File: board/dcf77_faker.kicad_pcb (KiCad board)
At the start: 4 copper layers, 69 x 32 mm, 50 parts, among them J1 Barrel_Jack, J2 DBG, J3 ANT, J4 LCD_I2C, SW1 RST, SW2 H, SW3 MIN, SW4 S, U1 NCP1117ST33T3G, U2 ATSAML21G18B-AUT, X1 32.768kHz, X2 31MHz

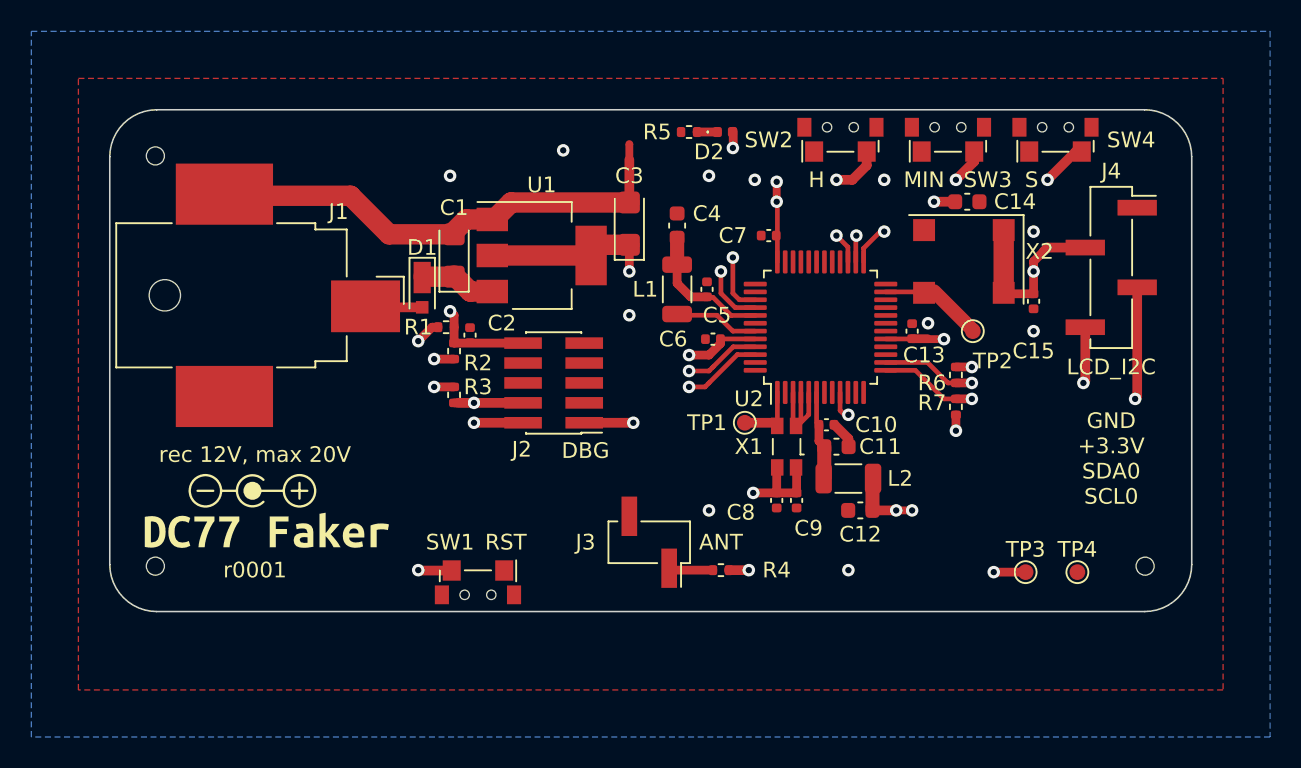
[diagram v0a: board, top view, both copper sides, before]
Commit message: hand-solder X2, fix newly-detected DRC violations
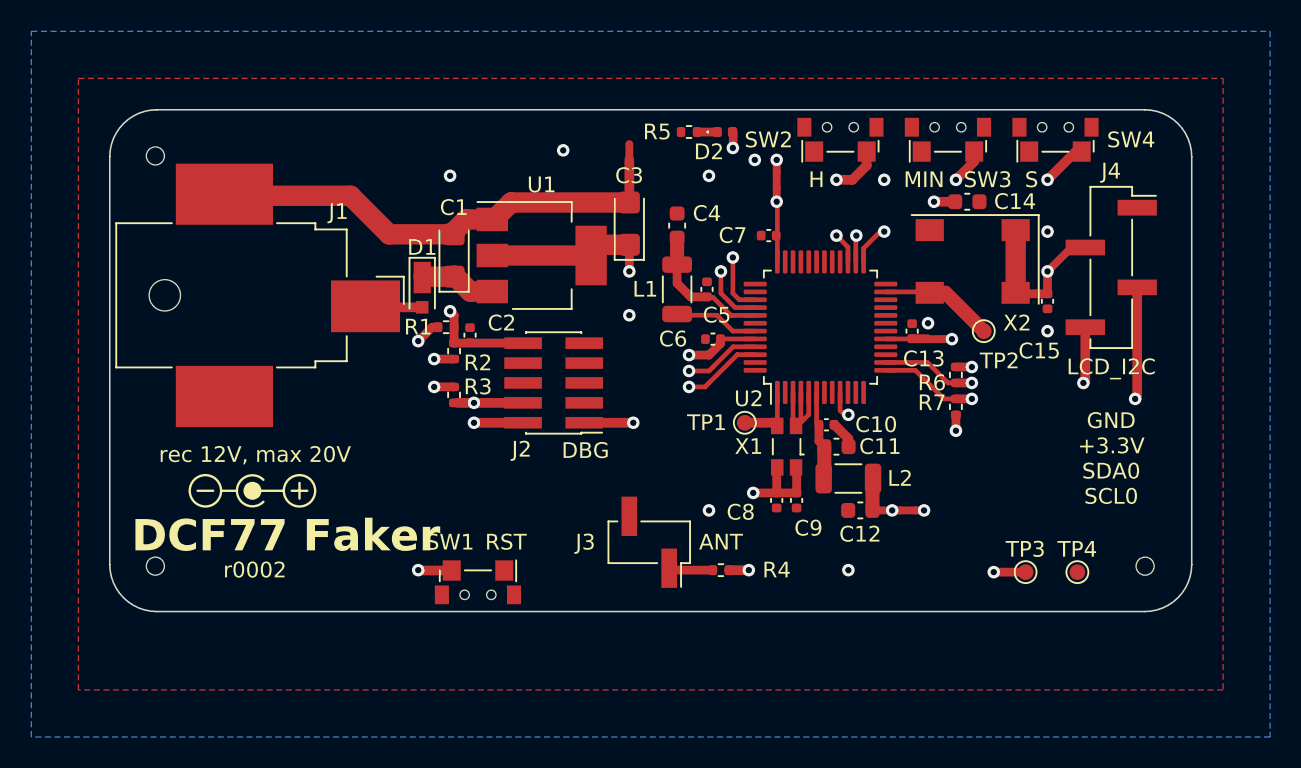
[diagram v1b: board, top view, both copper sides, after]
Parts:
- removed kibuzzard-1: G***, kibuzzard-639272B4
- X2: footprint Oscillator_Microchip:Oscillator_SMD_Microchip_DSC8001A-6Pin_7.0x5.0mm -> Oscillator_Microchip:Oscillator_SMD_Microchip_DSC8001A-6Pin_7.0x5.0mm_HandSolder
- moved C15 0.89 mm to (209.8, 69.2)
- moved NT2 0.77 mm to (192.5, 61.5)
- moved TP2 0.70 mm to (205.7, 71.1)
- moved X2 0.56 mm to (205.0, 66.7)
- moved NT3 0.24 mm to (200.9, 82.5)
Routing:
- net /VDDIO2: track 24.2 -> 25.8 mm
- net /XIN: track 5.53 -> 6.43 mm
- net +3.3V: track 37.9 -> 37.2 mm
- net /S: track 18.8 -> 19.3 mm
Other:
- board text added: "DCF77 Faker"
- board text added: "r0002"
- board text removed: "r0001"

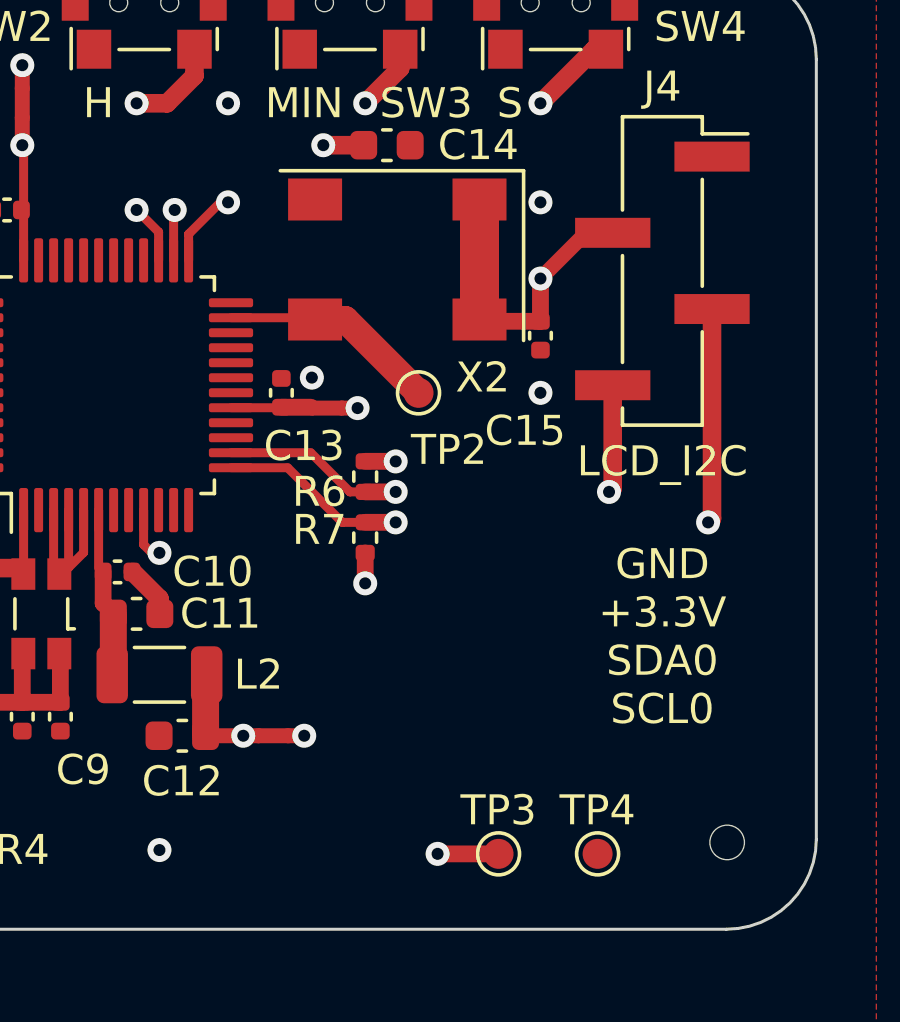
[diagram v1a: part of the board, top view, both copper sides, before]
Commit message: board: allow disabling X2
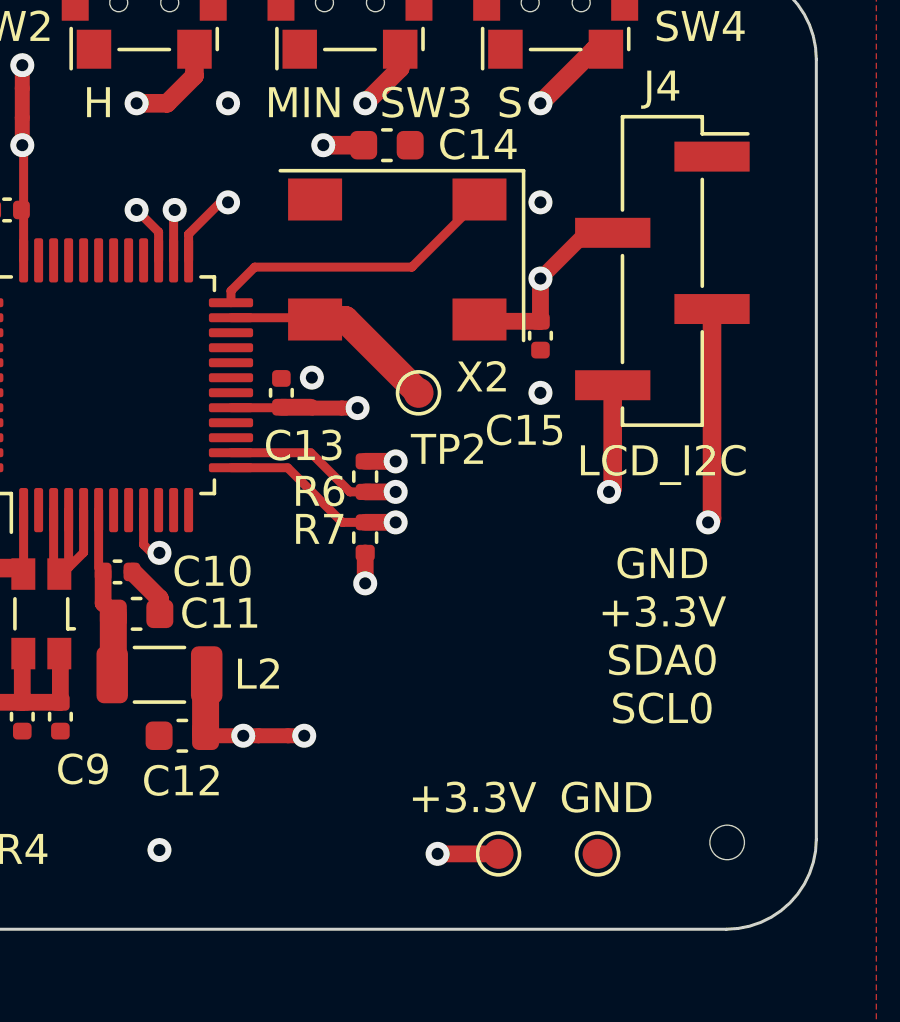
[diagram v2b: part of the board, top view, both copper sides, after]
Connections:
- U2 pad 24: unconnected-(U2-PA15-Pad24) -> /X~{ST}
- X2 pad 1: +3.3V -> /X~{ST}
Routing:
- net /X~{ST}: track 0.00 -> 9.94 mm
- net +3.3V: track 37.2 -> 33.3 mm
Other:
- board text added: "+3.3V"
- board text added: "GND"
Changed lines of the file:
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@@
   (net 3 "+3.3V")
   (net 4 "/VDDANA")
-  (net 5 "Net-(#FLG0102-pwr)")
+  (net 5 "Net-(D1-A)")
   (net 6 "Net-(D2-K)")
   (net 7 "/RAWGND")
@@
   (net 36 "unconnected-(U2-PA12-Pad21)")
   (net 37 "unconnected-(U2-PA13-Pad22)")
-  (net 38 "unconnected-(U2-PA15-Pad24)")
+  (net 38 "/X~{ST}")
   (net 39 "unconnected-(U2-PA19-Pad28)")
   (net 40 "unconnected-(U2-PA20-Pad29)")
@@
     (pad "" np_thru_hole circle (at 0 7 270) (size 2 2) (drill 2) (layers "*.Cu" "*.Mask"))
     (pad "1" smd rect (at 0.7 -5.8 270) (size 3.3 4.4) (layers "F.Cu" "F.Paste" "F.Mask")
-      (net 5 "Net-(#FLG0102-pwr)") (pintype "passive"))
+      (net 5 "Net-(D1-A)") (pintype "passive"))
     (pad "2" smd rect (at -6.45 3.2 270) (size 3.9 6.2) (layers "F.Cu" "F.Paste" "F.Mask")
       (net 7 "/RAWGND") (pintype "passive"))
@@
       (net 24 "/XIN") (pinfunction "PA14") (pintype "bidirectional"))
     (pad "24" smd roundrect (at 2.75 4.1625 90) (size 0.3 1.475) (layers "F.Cu" "F.Paste" "F.Mask") (roundrect_rratio 0.25)
-      (net 38 "unconnected-(U2-PA15-Pad24)") (pinfunction "PA15") (pintype "bidirectional+no_connect"))
+      (net 38 "/X~{ST}") (pinfunction "PA15") (pintype "bidirectional"))
     (pad "25" smd roundrect (at 4.1625 2.75 90) (size 1.475 0.3) (layers "F.Cu" "F.Paste" "F.Mask") (roundrect_rratio 0.25)
       (net 51 "/S") (pinfunction "PA16") (pintype "bidirectional"))
@@
       (net 2 "Net-(D1-K)") (pinfunction "K") (pintype "passive"))
     (pad "2" smd rect (at 1.02 0 270) (size 0.8 0.8) (layers "F.Cu" "F.Paste" "F.Mask")
-      (net 5 "Net-(#FLG0102-pwr)") (pinfunction "A") (pintype "passive"))
+      (net 5 "Net-(D1-A)") (pinfunction "A") (pintype "passive"))
     (model "${KICAD6_3DMODEL_DIR}/Diode_SMD.3dshapes/D_MicroSMP_AK.wrl"
       (offset (xyz 0 0 0))
@@
     (property "ki_keywords" "test point tp")
     (attr exclude_from_pos_files exclude_from_bom)
-    (fp_text reference "TP4" (at 0 -1.448) (layer "F.SilkS")
+    (fp_text reference "TP4" (at 0 -1.448) (layer "F.SilkS") hide
         (effects (font (size 1 1) (thickness 0.15)))
     )
@@
         (effects (font (size 1 1) (thickness 0.15)))
     )
-    (fp_text user "${REFERENCE}" (at 0 -1.45) (layer "F.Fab")
+    (fp_text user "${REFERENCE}" (at 0 1.651) (layer "F.Fab")
         (effects (font (size 1 1) (thickness 0.15)))
     )
@@
     (property "ki_keywords" "test point tp")
     (attr exclude_from_pos_files exclude_from_bom)
-    (fp_text reference "TP3" (at 0 -1.448) (layer "F.SilkS")
+    (fp_text reference "TP3" (at 0 -1.448) (layer "F.SilkS") hide
         (effects (font (size 1 1) (thickness 0.15)))
     )
@@
         (effects (font (size 1 1) (thickness 0.15)))
     )
-    (fp_text user "${REFERENCE}" (at 0 -1.45) (layer "F.Fab")
+    (fp_text user "${REFERENCE}" (at 0 1.651) (layer "F.Fab")
         (effects (font (size 1 1) (thickness 0.15)))
     )
@@
       (stroke (width 0.1) (type solid)) (layer "F.Fab"))
     (pad "1" smd rect (at -2 -2.74 270) (size 1.4 1.8) (layers "F.Cu" "F.Paste" "F.Mask")
-      (net 3 "+3.3V") (pinfunction "~{ST}") (pintype "input"))
+      (net 38 "/X~{ST}") (pinfunction "~{ST}") (pintype "input"))
     (pad "2" smd rect (at -2 2.74 270) (size 1.4 1.8) (layers "F.Cu" "F.Paste" "F.Mask")
       (net 1 "GND") (pinfunction "GND") (pintype "power_in"))
@@
     )
   )
+  (gr_text "+3.3V" (at 209.677 85.217) (layer "F.SilkS")
+    (effects (font (size 1 1) (thickness 0.15)) (justify right bottom))
+  )
   (gr_text "GND\n+3.3V\nSDA0\nSCL0" (at 213.868 79.248) (layer "F.SilkS")
     (effects (font (size 1 1) (thickness 0.15)))
@@
     (effects (font (size 1 1) (thickness 0.15)))
   )
+  (gr_text "GND" (at 210.439 85.217) (layer "F.SilkS")
+    (effects (font (size 1 1) (thickness 0.15)) (justify left bottom))
+  )
   (segment (start 193.576 75.0285) (end 193.576 76.934) (width 0.299974) (layer "F.Cu") (net 1))
   (segment (start 194.576 75.0285) (end 194.576 76.442) (width 0.299974) (layer "F.Cu") (net 1))
@@
   (segment (start 209.804 68.735) (end 207.832 68.735) (width 0.56007) (layer "F.Cu") (net 3))
   (segment (start 183.134 65.612) (end 180.768 65.612) (width 1.299972) (layer "F.Cu") (net 3))
-  (segment (start 207.772 64.675) (end 207.772 68.58) (width 1.299972) (layer "F.Cu") (net 3))
   (segment (start 193.802 81.435) (end 191.036 81.435) (width 0.56007) (layer "F.Cu") (net 3))
   (segment (start 192.532 60.96) (end 192.532 60.198) (width 0.5) (layer "F.Cu") (net 3))
@@
   (segment (start 192.576 75.0285) (end 192.576 77.045) (width 0.299974) (layer "F.Cu") (net 25))
   (segment (start 190.5 76.962) (end 192.405 76.962) (width 0.620014) (layer "F.Cu") (net 25))
+  (segment (start 199.4885 67.7195) (end 200.279 66.929) (width 0.3) (layer "F.Cu") (net 38))
+  (segment (start 205.518 66.929) (end 207.772 64.675) (width 0.3) (layer "F.Cu") (net 38))
+  (segment (start 200.279 66.929) (end 205.518 66.929) (width 0.3) (layer "F.Cu") (net 38))
+  (segment (start 199.4885 68.116) (end 199.4885 67.7195) (width 0.3) (layer "F.Cu") (net 38))
   (segment (start 191.1635 71.616) (end 188.988 71.616) (width 0.299974) (layer "F.Cu") (net 48))
   (segment (start 188.214 72.644) (end 187.198 72.644) (width 0.56007) (layer "F.Cu") (net 48))

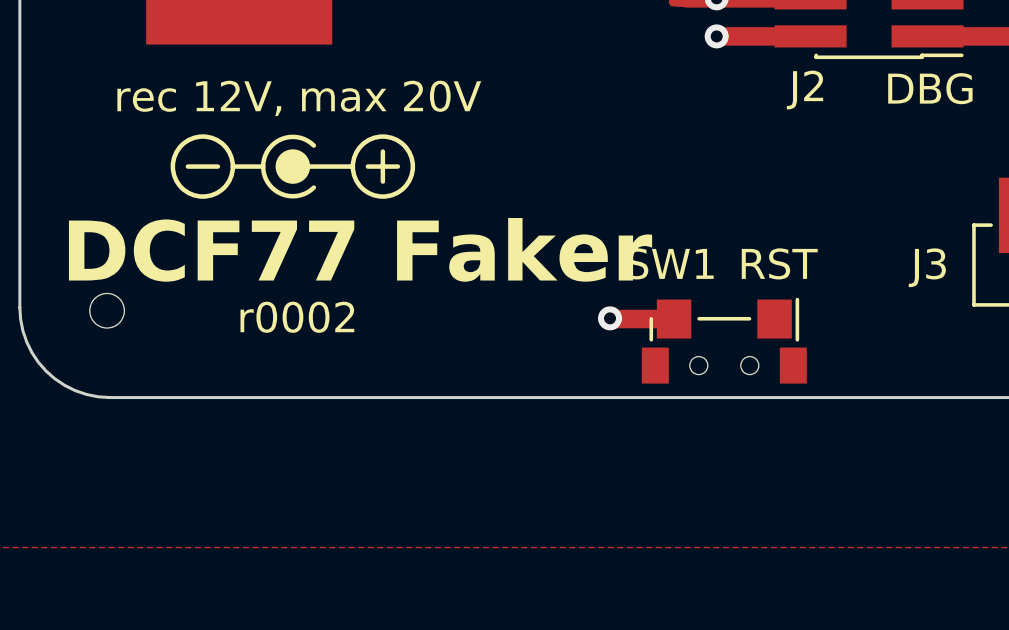
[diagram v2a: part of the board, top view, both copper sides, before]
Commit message: board: move RST to make space for battery input
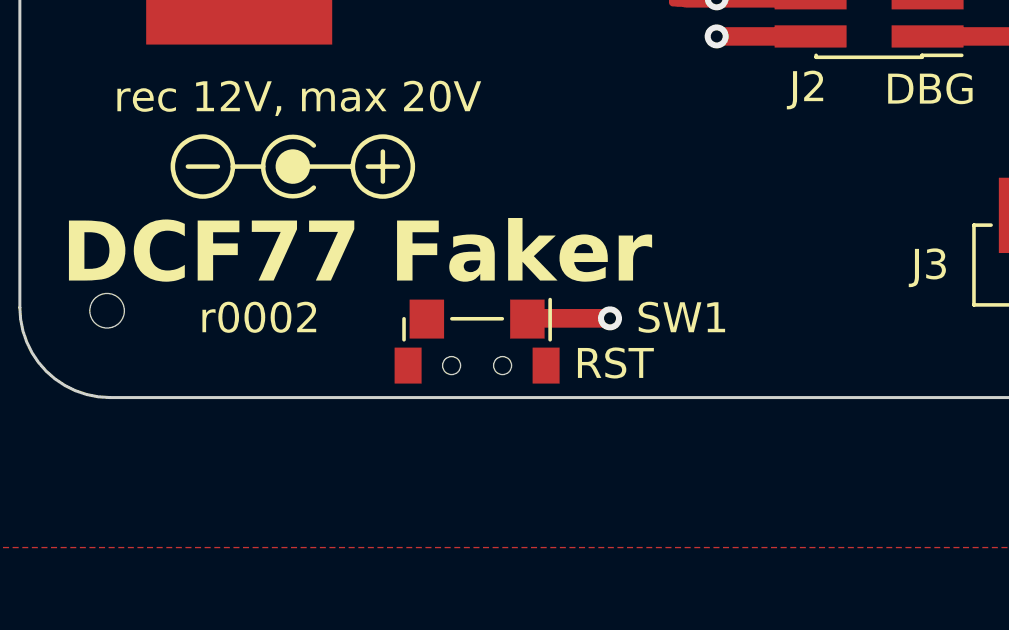
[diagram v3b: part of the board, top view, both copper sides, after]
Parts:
- moved SW1 8.24 mm to (165.2, 87.9)
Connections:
- SW1 pad 1: GND -> Net-(R2-Pad2)
- SW1 pad 2: Net-(R2-Pad2) -> GND
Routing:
- net Net-(R2-Pad2): track 17.3 -> 17.9 mm
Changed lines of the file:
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@@
   )
   (footprint "Button_Switch_SMD_Side:Shou_Han_TS24CA" (layer "F.Cu")
-    (at 173.482 87.884 180)
+    (at 165.241 87.884 180)
     (descr "Horizontal SMD button, https://datasheet.lcsc.com/lcsc/1912111437_SHOU-HAN-TS24CA_C393942.pdf")
     (property "LCSC" "C393942")
@@
     (property "ki_keywords" "switch normally-open pushbutton push-button")
     (attr smd)
-    (fp_text reference "SW1" (at 1.778 3.302 unlocked) (layer "F.SilkS")
-        (effects (font (size 1 1) (thickness 0.15)))
-    )
-    (fp_text value "RST" (at -1.778 3.302 unlocked) (layer "F.SilkS")
+    (fp_text reference "SW1" (at -6.844 1.524 unlocked) (layer "F.SilkS")
+        (effects (font (size 1 1) (thickness 0.15)))
+    )
+    (fp_text value "RST" (at -4.558 0 unlocked) (layer "F.SilkS")
         (effects (font (size 1 1) (thickness 0.15)))
     )
@@
     (pad "" np_thru_hole circle (at 0.85 -0.05 180) (size 0.6 0.6) (drill 0.6) (layers "F&B.Cu" "*.Mask"))
     (pad "1" smd rect (at -1.675 1.5 180) (size 1.15 1.3) (layers "F.Cu" "F.Paste" "F.Mask")
-      (net 1 "GND") (pinfunction "1") (pintype "passive"))
+      (net 22 "Net-(R2-Pad2)") (pinfunction "1") (pintype "passive"))
     (pad "2" smd rect (at 1.675 1.5 180) (size 1.15 1.3) (layers "F.Cu" "F.Paste" "F.Mask")
-      (net 22 "Net-(R2-Pad2)") (pinfunction "2") (pintype "passive"))
+      (net 1 "GND") (pinfunction "2") (pintype "passive"))
     (pad "3" smd rect (at -2.3 -0.05 180) (size 0.9 1.2) (layers "F.Cu" "F.Paste" "F.Mask"))
     (pad "3" smd rect (at 2.3 -0.05 180) (size 0.9 1.2) (layers "F.Cu" "F.Paste" "F.Mask"))
@@
     (effects (font (size 1 1) (thickness 0.15)))
   )
-  (gr_text "r0002" (at 159.258 86.36) (layer "F.SilkS")
+  (gr_text "r0002" (at 157.988 86.36) (layer "F.SilkS")
     (effects (font (size 1 1) (thickness 0.15)))
   )
@@
   (segment (start 169.696 86.384) (end 169.672 86.36) (width 0.620014) (layer "F.Cu") (net 22))
   (segment (start 171.958 72.9) (end 170.69 72.9) (width 0.56007) (layer "F.Cu") (net 22))
-  (segment (start 171.807 86.384) (end 169.696 86.384) (width 0.620014) (layer "F.Cu") (net 22))
+  (segment (start 169.672 86.36) (end 166.94 86.36) (width 0.620014) (layer "F.Cu") (net 22))
   (segment (start 170.69 72.9) (end 170.688 72.898) (width 0.56007) (layer "F.Cu") (net 22))
   (via (at 170.688 72.898) (size 0.8) (drill 0.4) (layers "F.Cu" "B.Cu") (net 22))
